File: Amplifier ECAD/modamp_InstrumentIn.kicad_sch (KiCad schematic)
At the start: 19 parts

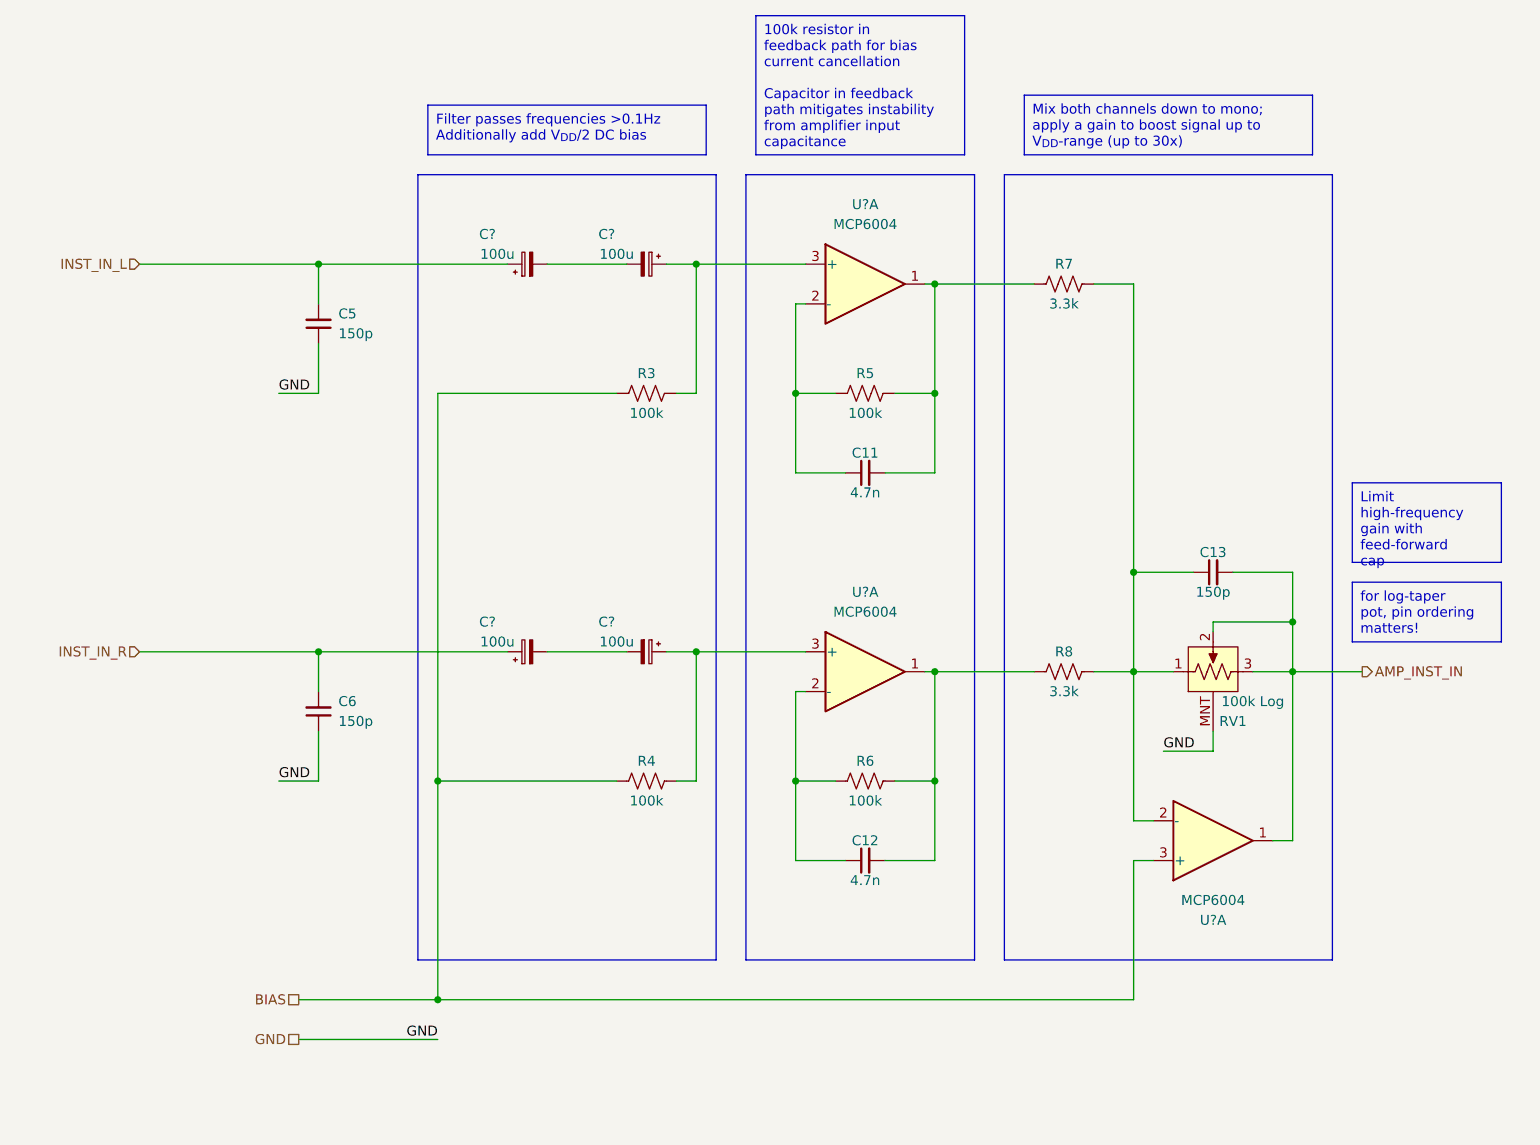
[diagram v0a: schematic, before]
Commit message: File renaming; updating supplier references
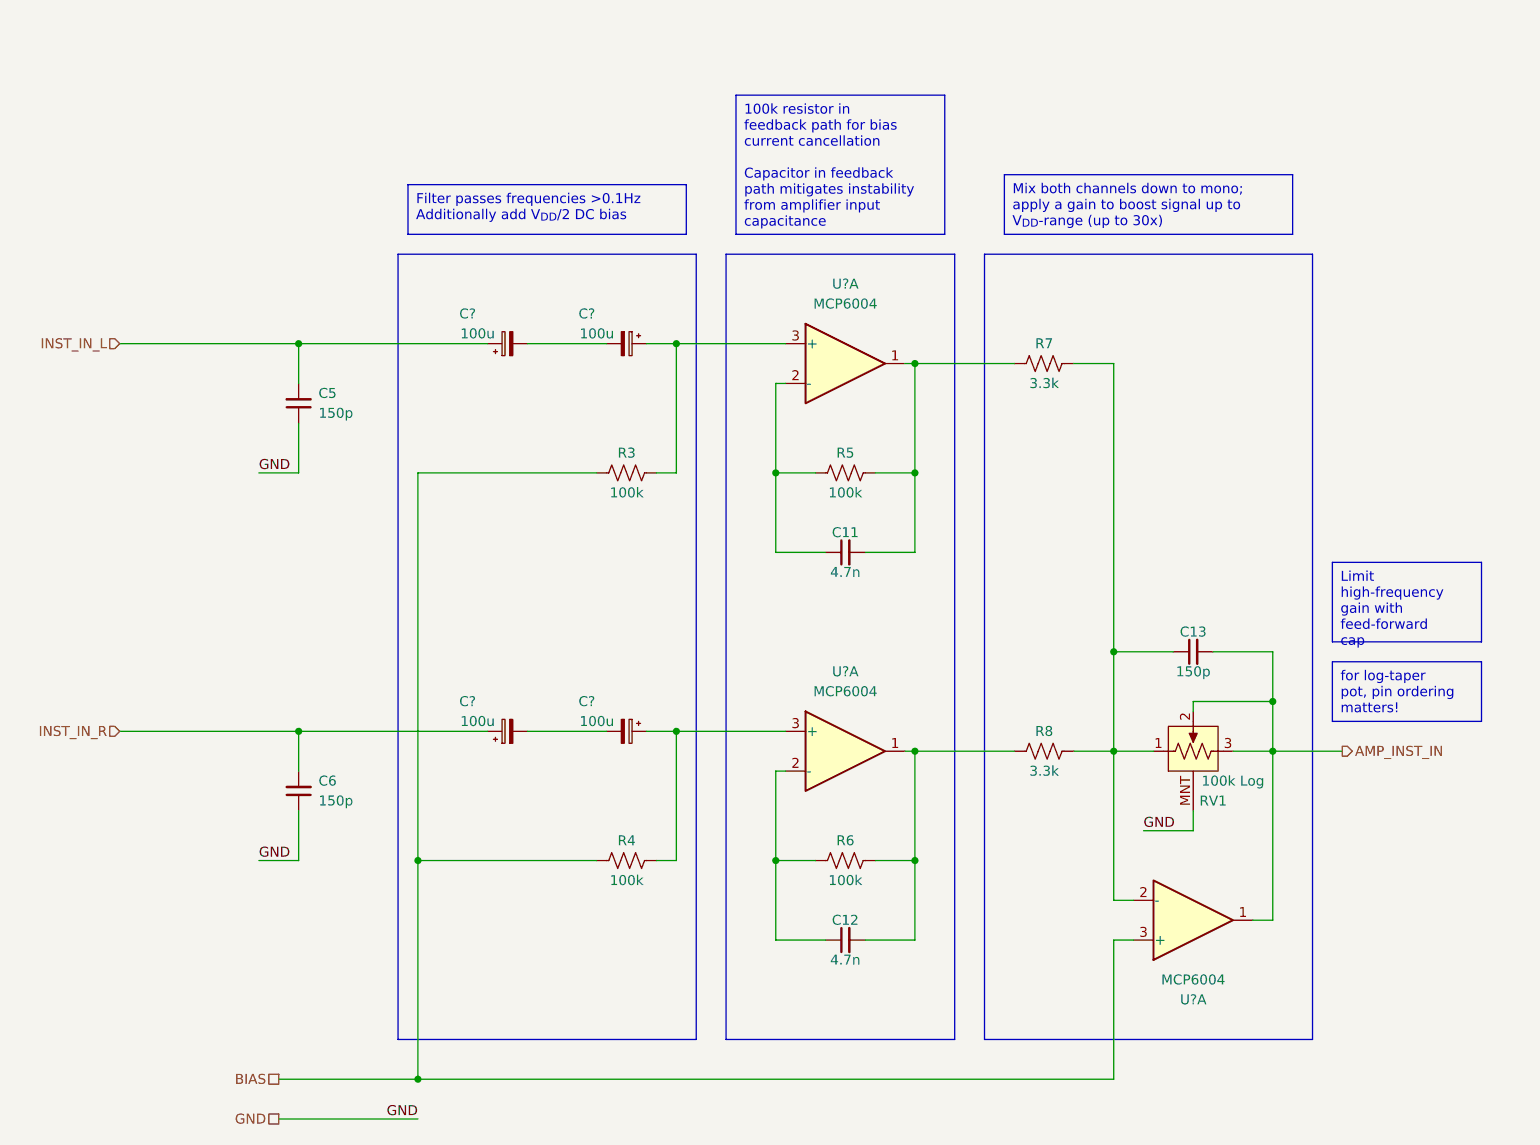
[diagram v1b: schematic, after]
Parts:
- C11, C12: footprint Custom-RLC:C_Disc_L7.2mm_W2.5mm_H6.6mm_P5.00mm_MODIFIED_1 -> Custom-RLC:C_KEMET_C322; symbol Custom-CapacitorTHT:FG28C0G2A472JRT06 -> Custom-CapacitorTHT:C322C472J1G5TA; Manufacturer TDK Corporation -> KEMET; Part Number FG28C0G2A472JRT06 -> C322C472J1G5TA
- C13, C5, C6: footprint Custom-RLC:C_Disc_L7.2mm_W2.5mm_H6.6mm_P5.00mm_MODIFIED_1 -> Custom-RLC:C_KEMET_C317; symbol Custom-CapacitorTHT:FG28C0G1H151JNT06 -> Custom-CapacitorTHT:C317C151J1G5TA; Manufacturer TDK Corporation -> KEMET; Part Number FG28C0G1H151JNT06 -> C317C151J1G5TA
- C? (x4): footprint Custom-RLC:CP_Radial_D6.3mm_H12.5_P2.50mm -> Custom-RLC:CP_KEMET_ESY; symbol Custom-CapacitorTHT:860020473008 -> Custom-CapacitorTHT:ESY107M025AE3AA; Manufacturer Würth Elektronik -> KEMET; Part Number 860020473008 -> ESY107M025AE3AA
- R3, R4, R5, R6: symbol Custom-ResistorTHT:MFR-25FRF52-100K -> Custom-ResistorTHT:CF14JT100K; Manufacturer YAGEO -> Stackpole Electronics Inc; Part Number MFR-25FRF52-100K -> CF14JT100K
- R7, R8: symbol Custom-ResistorTHT:MFR-25FRF52-3K3 -> Custom-ResistorTHT:CF14JT3K30; Manufacturer YAGEO -> Stackpole Electronics Inc; Part Number MFR-25FRF52-3K3 -> CF14JT3K30
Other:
- moved on the sheet: C11, C12, C13, C5, C6, C?, R3, R4, R5, R6, R7, R8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
